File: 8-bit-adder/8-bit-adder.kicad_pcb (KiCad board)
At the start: 2 copper layers, 109.2 x 88.9 mm, 227 parts, among them J1 J2-2_pole_connector, J2 J1-1_bit_bus, J3 J8-8_bit_bus_connector, J4 J8-8_bit_bus_connector, J5 J1-1_bit_bus, J6 J8-8_bit_bus_connector, Q1 2N7000, Q10 2N7000, Q100 2N7000, Q101 2N7000, Q102 2N7000, Q103 2N7000, Q104 2N7000, Q105 2N7000, Q106 2N7000, Q107 2N7000, Q108 2N7000, Q109 2N7000, Q11 2N7000, Q110 2N7000, Q111 2N7000, Q112 2N7000, Q113 2N7000, Q114 2N7000, Q115 2N7000, Q116 2N7000, Q117 2N7000, Q118 2N7000, Q119 2N7000, Q12 2N7000, Q120 2N7000, Q121 2N7000, Q122 2N7000, Q123 2N7000, Q124 2N7000, Q125 2N7000, Q126 2N7000, Q127 2N7000, Q128 2N7000, Q13 2N7000, Q14 2N7000, Q15 2N7000, Q16 2N7000, Q17 2N7000, Q18 2N7000, Q19 2N7000, Q2 2N7000, Q20 2N7000, Q21 2N7000, Q22 2N7000, Q23 2N7000, Q24 2N7000, Q25 2N7000, Q26 2N7000, Q27 2N7000, Q28 2N7000, Q29 2N7000, Q3 2N7000, Q30 2N7000, Q31 2N7000, Q32 2N7000, Q33 2N7000, Q34 2N7000, Q35 2N7000, Q36 2N7000, Q37 2N7000, Q38 2N7000, Q39 2N7000, Q4 2N7000, Q40 2N7000, Q41 2N7000, Q42 2N7000, Q43 2N7000, Q44 2N7000, Q45 2N7000, Q46 2N7000, Q47 2N7000, Q48 2N7000, Q49 2N7000, Q5 2N7000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

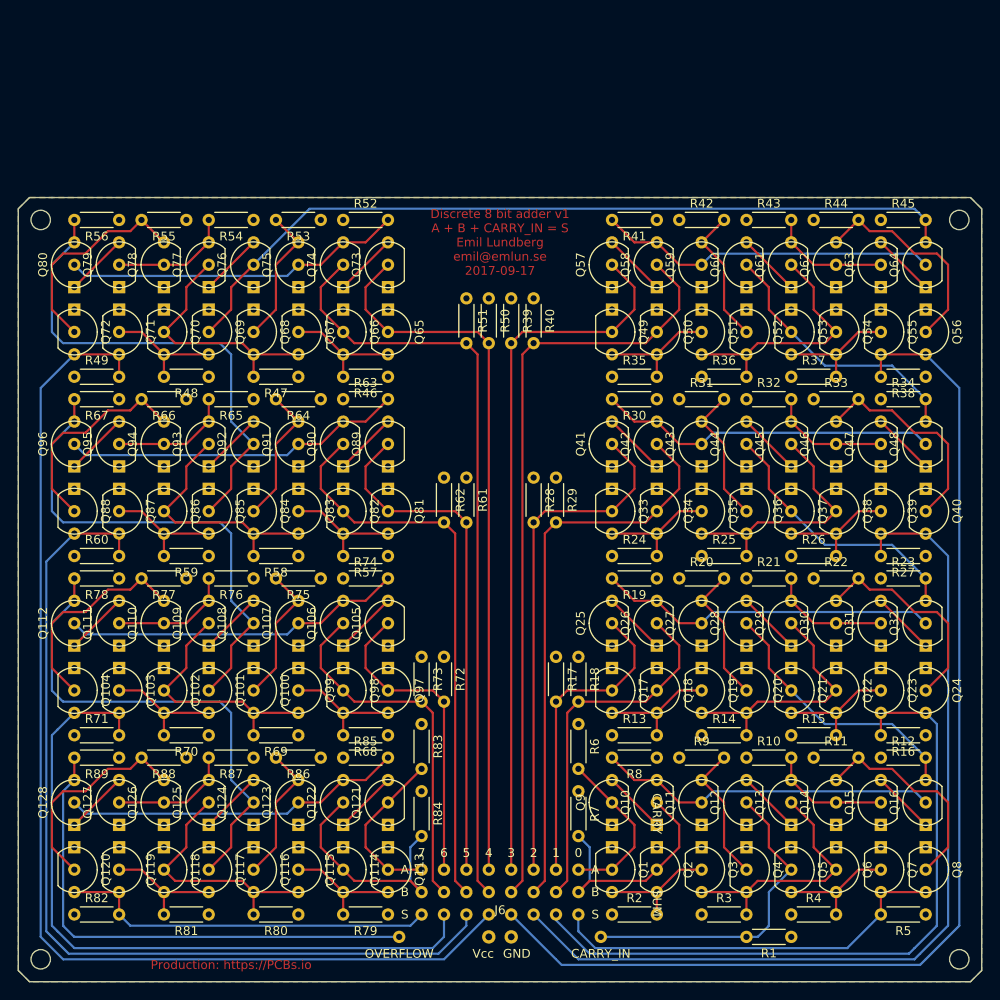
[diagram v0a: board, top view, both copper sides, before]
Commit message: Update adder circuit to revision 2
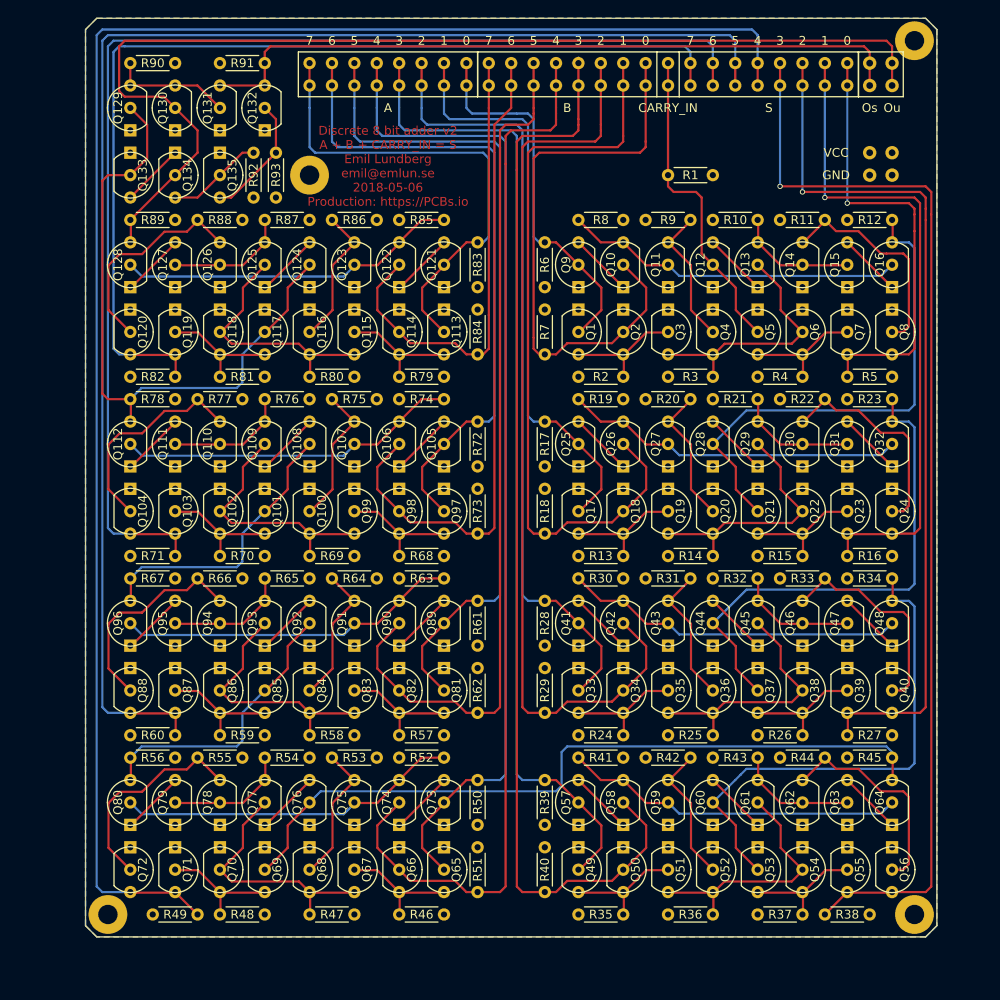
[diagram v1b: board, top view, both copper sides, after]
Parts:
- removed the REF** at (210.8, 147.3)
- removed the REF** at (210.8, 63.5)
- removed the REF** at (106.7, 63.5)
- removed the REF** at (106.7, 147.3)
- added Q129: 2N7000, electrokit:TO-92_Molded_Wide_Inline, F.Cu at (116.8, 50.8)
- added Q130: 2N7000, electrokit:TO-92_Molded_Wide_Inline, F.Cu at (121.9, 50.8)
- added Q131: 2N7000, electrokit:TO-92_Molded_Wide_Inline, F.Cu at (127.0, 50.8)
- added Q132: 2N7000, electrokit:TO-92_Molded_Wide_Inline, F.Cu at (132.1, 50.8)
- added Q133: 2N7000, electrokit:TO-92_Molded_Wide_Inline, F.Cu at (116.8, 58.4)
- added Q134: 2N7000, electrokit:TO-92_Molded_Wide_Inline, F.Cu at (121.9, 58.4)
- added Q135: 2N7000, electrokit:TO-92_Molded_Wide_Inline, F.Cu at (127.0, 58.4)
- added R90: 1M, emlun:R_Axial_DIN0204_L3.6mm_D1.6mm_P5.08mm_Horizontal, F.Cu at (121.9, 45.7)
- added R91: 1M, emlun:R_Axial_DIN0204_L3.6mm_D1.6mm_P5.08mm_Horizontal, F.Cu at (127.0, 45.7)
- added R92: 1M, emlun:R_Axial_DIN0204_L3.6mm_D1.6mm_P5.08mm_Horizontal, F.Cu at (130.8, 61.0)
- added R93: 1M, emlun:R_Axial_DIN0204_L3.6mm_D1.6mm_P5.08mm_Horizontal, F.Cu at (133.3, 61.0)
- added REF**: MountingHole_2.2mm_M2_Pad, Mounting_Holes:MountingHole_2.2mm_M2_Pad, F.Cu at (205.7, 43.2)
- added REF**: MountingHole_2.2mm_M2_Pad, Mounting_Holes:MountingHole_2.2mm_M2_Pad, F.Cu at (114.3, 142.2)
- added REF**: MountingHole_2.2mm_M2_Pad, Mounting_Holes:MountingHole_2.2mm_M2_Pad, F.Cu at (205.7, 142.2)
- added REF**: MountingHole_2.2mm_M2_Pad, Mounting_Holes:MountingHole_2.2mm_M2_Pad, F.Cu at (137.2, 58.4)
- J1: value J2-2_pole_connector -> PWR-2_pole_power_connector; footprint emlun:J2-2_pole_connector -> emlun:J2x2-double_2_pole_connector
- J2: footprint emlun:J1-1_bit_bus -> emlun:J1x2-double_1_bit_bus
- J3, J4, J6: footprint emlun:J8-8_bit_bus_connector -> emlun:J8x2-double_8_bit_bus_connector
- J5: value J1-1_bit_bus -> J2-2_bit_bus; footprint emlun:J1-1_bit_bus -> emlun:J2x2-double_2_bit_bus
- R1, R10, R11, R12, R13, R14, R15, R16, R17, R18, R19, R2, R20, R21, R22, R23, R24, R25, R26, R27, R28, R29, R3, R30, R31, R32, R33, R34, R35, R36, R37, R38, R39, R4, R40, R41, R42, R43, R44, R45, R46, R47, R48, R49, R5, R50, R51, R52, R53, R54, R55, R56, R57, R58, R59, R6, R60, R61, R62, R63, R64, R65, R66, R67, R68, R69, R7, R70, R71, R72, R73, R74, R75, R76, R77, R78, R79, R8, R80, R81, R82, R83, R84, R85, R86, R87, R88, R89, R9: footprint Resistors_THT:R_Axial_DIN0204_L3.6mm_D1.6mm_P5.08mm_Horizontal -> emlun:R_Axial_DIN0204_L3.6mm_D1.6mm_P5.08mm_Horizontal
- moved J5 113.7 mm to (203.2, 48.3)
- moved J4 104.2 mm to (198.1, 48.3)
- moved J2 96.8 mm to (177.8, 50.8)
- moved J1 96.0 mm to (200.7, 58.4), turned to 90 degrees
- moved J6 95.4 mm to (175.3, 48.3)
- moved J3 91.5 mm to (154.9, 48.3)
- moved R1 86.8 mm to (182.9, 58.4)
- moved Q123 62.6 mm to (142.2, 68.6)
- moved Q125 62.6 mm to (132.1, 68.6)
- moved Q127 62.6 mm to (121.9, 68.6)
- moved Q128 62.6 mm to (116.8, 68.6)
- moved Q121 62.6 mm to (152.4, 68.6)
- moved Q122 62.6 mm to (147.3, 68.6)
- moved Q124 62.6 mm to (137.2, 68.6)
- moved Q126 62.6 mm to (127.0, 68.6)
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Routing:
- net /Os: track 0.00 -> 81.8 mm
- net /S7: track 43.0 -> 113.2 mm
- net /C7: track 58.2 -> 124.3 mm
- net /S4: track 129.2 -> 190.4 mm
- net /S5: track 105.3 -> 164.0 mm
- net /S6: track 81.4 -> 138.6 mm
- net /b1: track 41.8 -> 84.6 mm
- net /b2: track 64.6 -> 103.6 mm
- net /a6: track 35.7 -> 74.4 mm
- net /b0: track 27.1 -> 65.5 mm
- net /a7: track 18.9 -> 55.4 mm
- net /b3: track 87.5 -> 123.6 mm
- net /a5: track 58.5 -> 93.5 mm
- net /b5: track 64.6 -> 98.6 mm
- net /b4: track 87.5 -> 121.4 mm
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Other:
- board size 109.2 x 88.9 mm -> 96.5 x 104.1 mm
- board text added: "Discrete 8 bit adder v2 A + B + CARRY_IN = S Emil Lundberg emil@emlun.se 2018-05-06 Production: https://PCBs.io"
- board text added: "Os"
- board text added: "Ou"
- board text added: "VCC"
- board text removed: "CARRY"
- board text removed: "Discrete 8 bit adder v1 A + B + CARRY_IN = S Emil Lundberg emil@emlun.se 2017-09-17"
- board text removed: "OVERFLOW"
- board text removed: "Production: https://PCBs.io"
- board text removed: "SUM"
- board text removed: "Vcc"
